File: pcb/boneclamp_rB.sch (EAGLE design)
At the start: 68 parts, among them IC1 24C, U1 ADA4841-2YRZ, U2 LT1964ES5-5TRMPBF, U3 ADA4841-2YRZ, U4 TLV70245DBVT, U5 ADA4841-2YRZ, U6 ADA4841-2YRZ, U7 AD7682BCPZ, U8 TPS63700DRCT, U9 ADA4841-2YRZ

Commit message: Finished basic ADC module
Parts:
- removed C1, C2, C3, C4: 1 uF, rcl:C-EUC0402
- removed JP2: (no value), jumper:JP2E
- removed JP3, JP4: (no value), jumper:JP1E
- removed U3, U5, U6: ADA4841-2YRZ, analog-devices-01:ADA4841-2YRZ
- added C10, C11: 10uF, rcl:C-EUC0805
- added C12, C13, C14: 0.1uF, rcl:C-EUC0805
- added R14: 1k, resistor:R-US_R0805
- added SJ6: (no value), jumper:SJ
- U1: value ADA4841-2YRZ -> AD8031ARTZ-R2; device analog-devices-01:ADA4841-2YRZ -> analog-devices-01:AD8031ARTZ-R2
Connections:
- net SDIN_BB renamed DAC_SDI
- net SDIN_DC renamed DAC_SDID
- net SDO_DC renamed DAC_SDO
- removed net N$1: U3.+VS, U5.+VS
- removed net N$13: C4.1
- removed net N$15: U3.OUT1, U5.OUT1
- removed net N$2: U3.+IN1, U5.+IN1
- removed net N$20: JP3.1
- removed net N$24: JP4.1, U$42.VREF
- removed net N$26: U3.OUT2, U5.OUT2
- removed net N$3: U3.-IN1, U5.-IN1
- removed net N$4: U3.+IN2, U5.+IN2
- removed net N$5: U3.-IN2, U5.-IN2
- removed net N$6: U3.-VS, U5.-VS
- removed net VREF_2.5V: JP3.2, JP4.2
- new net ADC_SDO: SJ6.2
- new net N$28: C11.1, R14.2, U7.REF
- new net N$29: C10.1, R14.1, U1.+IN
- new net N$34: C14.1, U7.REFIN
- new net VCOM: U7.COM
- new net VREF: U1.-IN, U1.VOUT
- new net _ADC_A: U7.IN0
- new net _ADC_B: U7.IN1
- new net _ADC_C: U7.IN2
- new net _ADC_D: U7.IN3
- net AGND: now also C10.2, C11.2, C12.2, C13.2, C14.2, U1.-VS, U7.EP, U7.GND, U7.GND_2; no longer C1.2, C2.2, C3.2, C4.2
- net DGND: no longer JP2.3
- net N$10: now also U7.SCK; no longer C2.1
- net N$11: now also U7.DIN; no longer C1.1
- net N$12: now also U7.CNV; no longer JP2.2
- net N$9: now also SJ6.1; no longer C3.1
- net VDD: now also C13.1, U1.+VS, U7.VDD, U7.VDD_2
- net VDRIVE: now also C12.1, U7.VIO; no longer JP2.1
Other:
- moved on the sheet: U7, U9

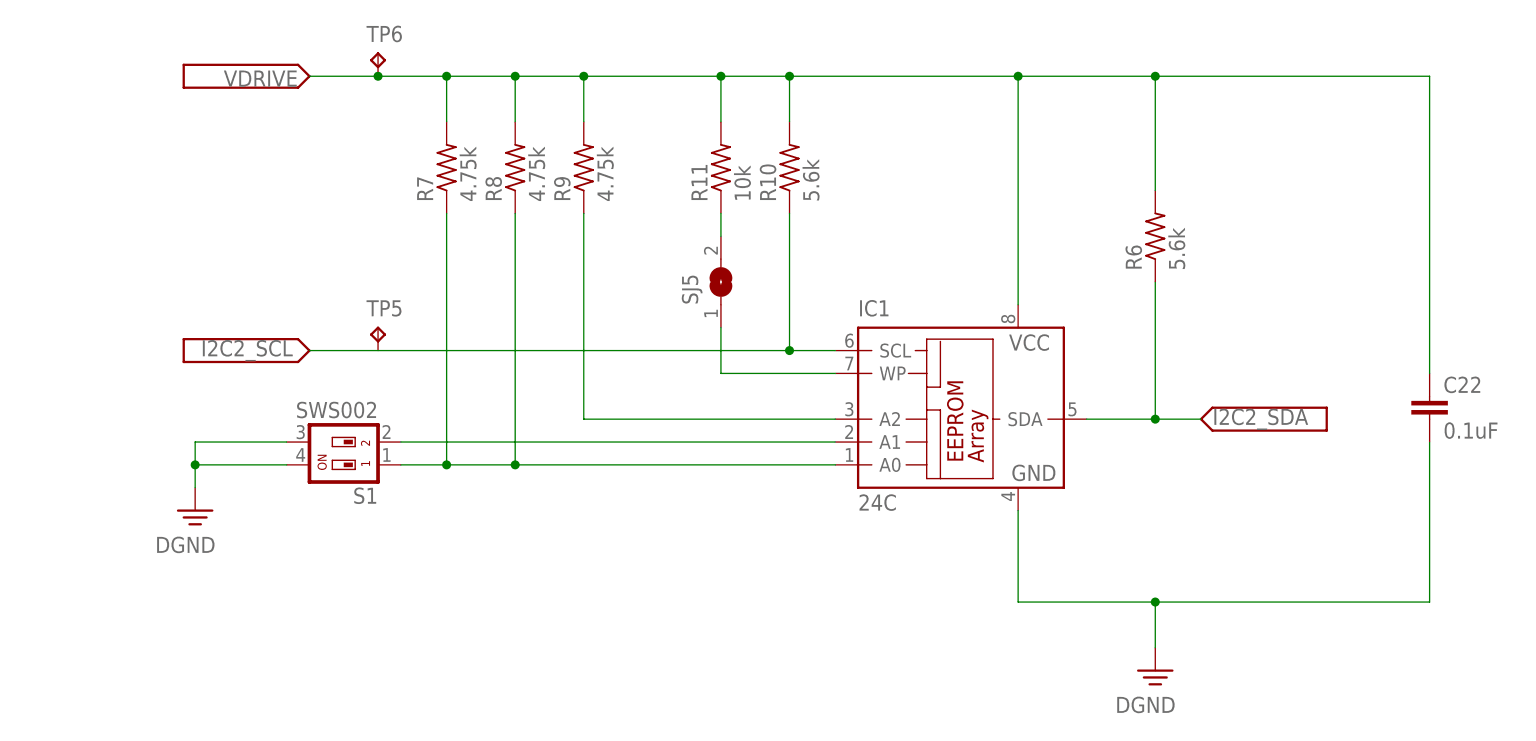
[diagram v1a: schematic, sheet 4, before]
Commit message: Added buffered VREF divider, which feeds back into ADC to get bipolar input swing.
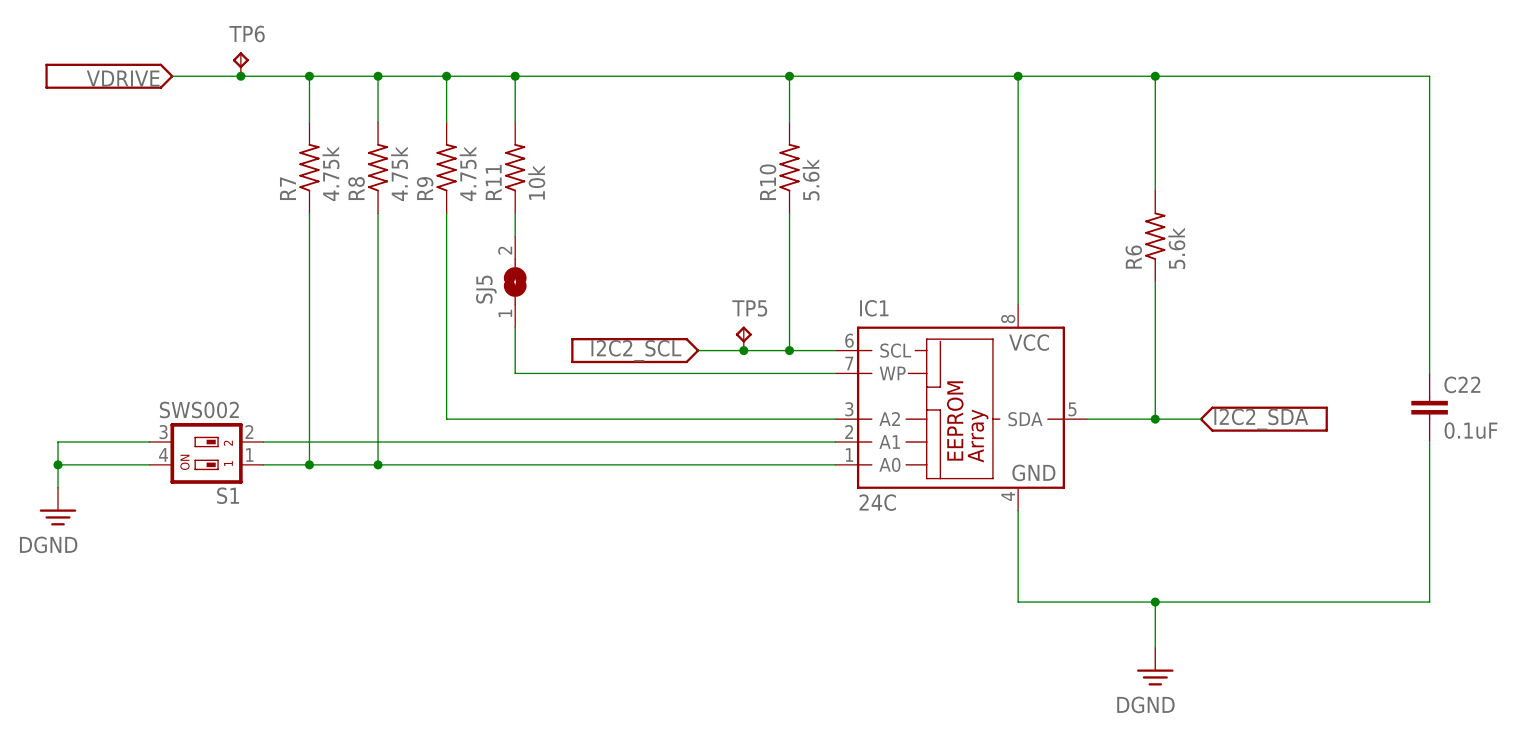
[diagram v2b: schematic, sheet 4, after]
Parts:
- added C1: 10uF, rcl:C-EUC0805
- added R15, R16: 10k,1%, resistor:R-US_R0805
- U1: value AD8031ARTZ-R2 -> AD8032ARZ-REEL7; device analog-devices-01:AD8031ARTZ-R2 -> analog-devices-02:AD8032ARZ-REEL7
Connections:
- new net N$4: C1.1, R15.2, R16.1, U1.+IN2
- net AGND: now also C1.2, R16.2
- net I2C2_SCL: now also TP5.TP
- net N$29: now also U1.+IN1; no longer U1.+IN
- net VCOM: now also U1.-IN2, U1.OUT2
- net VREF: now also R15.1, U1.-IN1, U1.OUT1; no longer U1.-IN, U1.VOUT
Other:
- moved on the sheet: C10, C11, C14, R11, R7, R8, R9, S1, SJ5, TP5, TP6

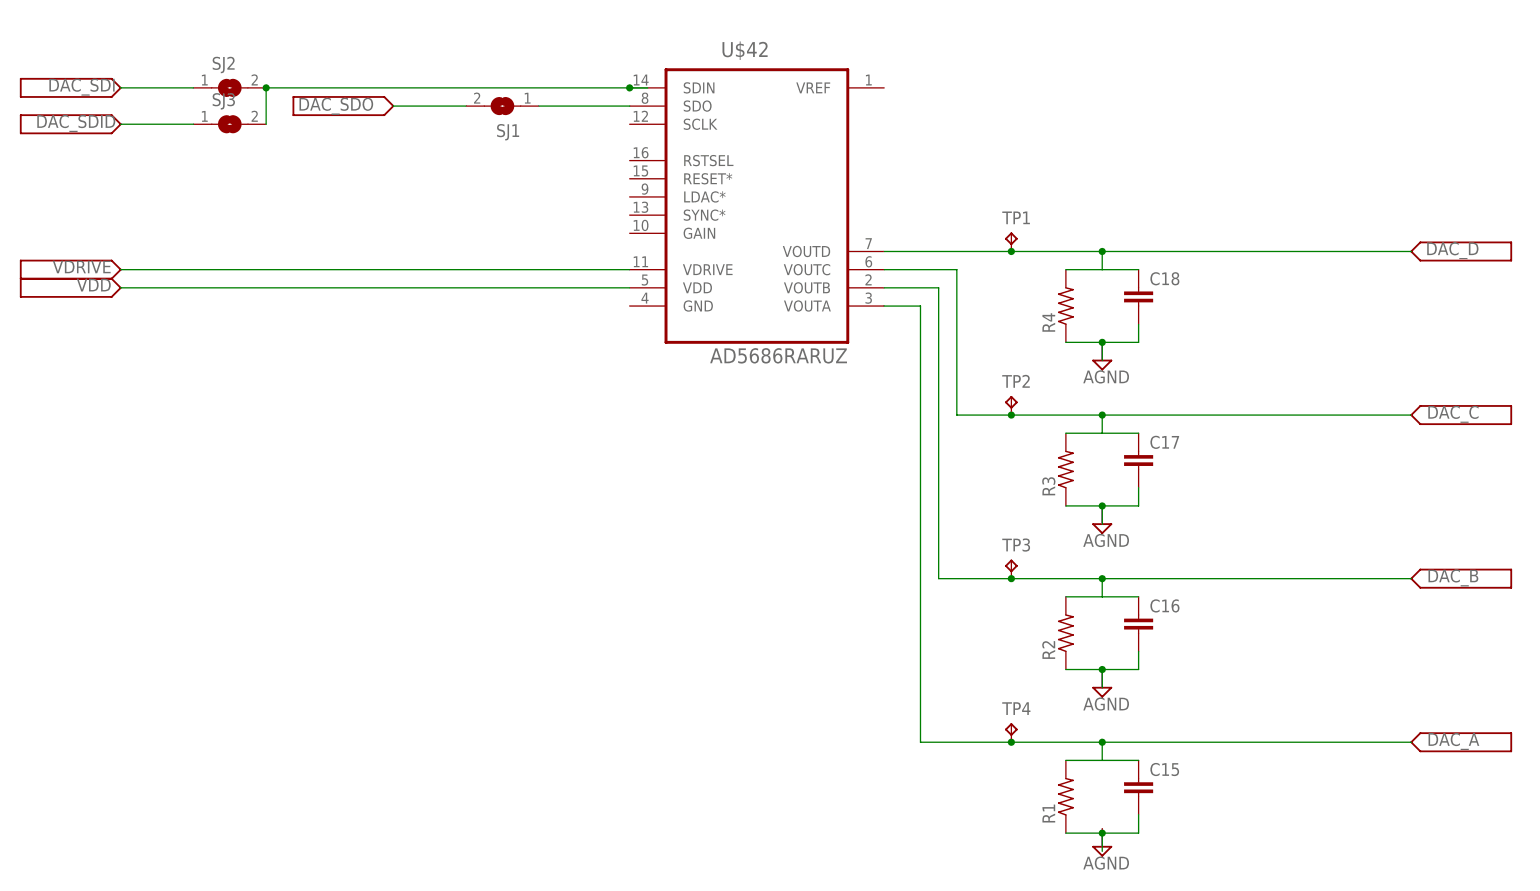
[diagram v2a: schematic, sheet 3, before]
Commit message: Finished digital input to DAC
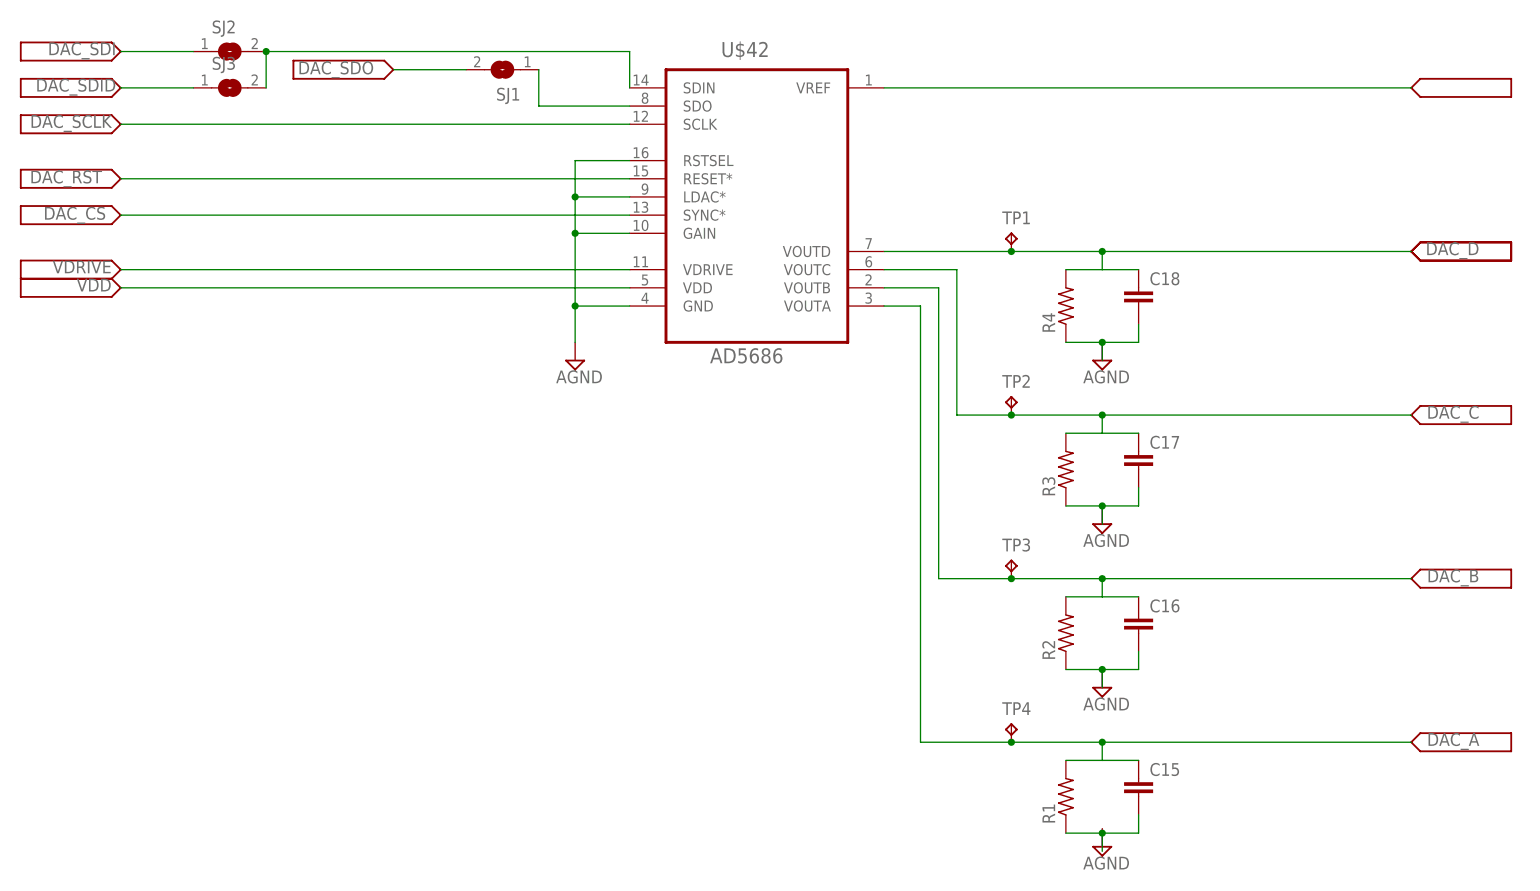
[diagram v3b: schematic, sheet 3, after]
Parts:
- added SJ7, SJ8: (no value), jumper:SJ
- U$42: value AD5686RARUZ -> AD5686
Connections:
- net N$10 renamed ADC_SCLK
- new net ADC_SDI: SJ7.1
- new net ADC_SDID: SJ8.1
- new net DAC_CS: U$42.SYNC*
- new net DAC_RST: U$42.RESET*
- new net DAC_SCLK: U$42.SCLK
- net AGND: now also U$42.GAIN, U$42.GND, U$42.LDAC*, U$42.RSTSEL
- net N$11: now also SJ7.2, SJ8.2
- net VREF: now also U$42.VREF
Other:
- moved on the sheet: C14, SJ1, SJ2, SJ3, U9

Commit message: Minor schematic edit
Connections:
- new net _DAC_A: C15.1, R1.2, TP4.TP, U$42.VOUTA
- new net _DAC_B: C16.1, R2.2, TP3.TP, U$42.VOUTB
- new net _DAC_C: C17.1, R3.2, TP2.TP, U$42.VOUTC
- new net _DAC_D: C18.1, R4.2, TP1.TP, U$42.VOUTD
- net DAC_A: no longer C15.1, R1.2, TP4.TP, U$42.VOUTA
- net DAC_B: no longer C16.1, R2.2, TP3.TP, U$42.VOUTB
- net DAC_C: no longer C17.1, R3.2, TP2.TP, U$42.VOUTC
- net DAC_D: no longer C18.1, R4.2, TP1.TP, U$42.VOUTD
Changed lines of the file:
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@@
 </busses>
 <nets>
-<net name="DAC_A" class="0">
-<segment>
-<wire x1="17.78" y1="-15.24" x2="22.86" y2="-15.24" width="0.1524" layer="91"/>
-<label x="100.965" y="-74.93" size="1.778" layer="95" rot="R180"/>
-<wire x1="22.86" y1="-15.24" x2="22.86" y2="-76.2" width="0.1524" layer="91"/>
-<wire x1="22.86" y1="-76.2" x2="35.56" y2="-76.2" width="0.1524" layer="91"/>
-<pinref part="R1" gate="G$1" pin="2"/>
-<pinref part="C15" gate="G$1" pin="1"/>
-<wire x1="35.56" y1="-76.2" x2="48.26" y2="-76.2" width="0.1524" layer="91"/>
-<wire x1="48.26" y1="-76.2" x2="91.44" y2="-76.2" width="0.1524" layer="91"/>
-<wire x1="48.26" y1="-78.74" x2="53.34" y2="-78.74" width="0.1524" layer="91"/>
-<wire x1="43.18" y1="-78.74" x2="48.26" y2="-78.74" width="0.1524" layer="91"/>
-<wire x1="48.26" y1="-78.74" x2="48.26" y2="-76.2" width="0.1524" layer="91"/>
-<junction x="48.26" y="-76.2"/>
-<pinref part="TP4" gate="G$1" pin="TP"/>
-<junction x="35.56" y="-76.2"/>
-<pinref part="U$42" gate="G$1" pin="VOUTA"/>
-</segment>
-</net>
-<net name="DAC_B" class="0">
-<segment>
-<pinref part="R2" gate="G$1" pin="2"/>
-<pinref part="C16" gate="G$1" pin="1"/>
-<wire x1="48.26" y1="-55.88" x2="53.34" y2="-55.88" width="0.1524" layer="91"/>
-<wire x1="43.18" y1="-55.88" x2="48.26" y2="-55.88" width="0.1524" layer="91"/>
-<wire x1="48.26" y1="-55.88" x2="48.26" y2="-53.34" width="0.1524" layer="91"/>
-<wire x1="17.78" y1="-12.7" x2="25.4" y2="-12.7" width="0.1524" layer="91"/>
-<wire x1="25.4" y1="-12.7" x2="25.4" y2="-53.34" width="0.1524" layer="91"/>
-<wire x1="25.4" y1="-53.34" x2="35.56" y2="-53.34" width="0.1524" layer="91"/>
-<wire x1="35.56" y1="-53.34" x2="48.26" y2="-53.34" width="0.1524" layer="91"/>
-<wire x1="48.26" y1="-53.34" x2="91.44" y2="-53.34" width="0.1524" layer="91"/>
-<junction x="48.26" y="-53.34"/>
-<label x="100.965" y="-52.07" size="1.778" layer="95" rot="R180"/>
-<pinref part="TP3" gate="G$1" pin="TP"/>
-<junction x="35.56" y="-53.34"/>
-<pinref part="U$42" gate="G$1" pin="VOUTB"/>
-</segment>
-</net>
 <net name="N$7" class="0">
 <segment>
@@
 </segment>
 </net>
-<net name="DAC_C" class="0">
+<net name="VREF" class="0">
+<segment>
+<pinref part="U$42" gate="G$1" pin="VREF"/>
+<wire x1="17.78" y1="15.24" x2="91.44" y2="15.24" width="0.1524" layer="91"/>
+<label x="92.71" y="14.605" size="1.778" layer="95"/>
+</segment>
+</net>
+<net name="DAC_SCLK" class="0">
+<segment>
+<pinref part="U$42" gate="G$1" pin="SCLK"/>
+<wire x1="-17.78" y1="10.16" x2="-88.9" y2="10.16" width="0.1524" layer="91"/>
+<label x="-90.17" y="11.43" size="1.778" layer="95" rot="R180"/>
+</segment>
+</net>
+<net name="DAC_RST" class="0">
+<segment>
+<pinref part="U$42" gate="G$1" pin="RESET*"/>
+<wire x1="-17.78" y1="2.54" x2="-88.9" y2="2.54" width="0.1524" layer="91"/>
+<label x="-101.6" y="1.905" size="1.778" layer="95"/>
+</segment>
+</net>
+<net name="DAC_CS" class="0">
+<segment>
+<pinref part="U$42" gate="G$1" pin="SYNC*"/>
+<wire x1="-88.9" y1="-2.54" x2="-17.78" y2="-2.54" width="0.1524" layer="91"/>
+<label x="-99.695" y="-3.175" size="1.778" layer="95"/>
+</segment>
+</net>
+<net name="_DAC_D" class="0">
+<segment>
+<wire x1="17.78" y1="-7.62" x2="35.56" y2="-7.62" width="0.1524" layer="91"/>
+<label x="102.87" y="-6.35" size="1.778" layer="95" rot="R180"/>
+<pinref part="R4" gate="G$1" pin="2"/>
+<pinref part="C18" gate="G$1" pin="1"/>
+<wire x1="48.26" y1="-10.16" x2="53.34" y2="-10.16" width="0.1524" layer="91"/>
+<wire x1="43.18" y1="-10.16" x2="48.26" y2="-10.16" width="0.1524" layer="91"/>
+<wire x1="48.26" y1="-10.16" x2="48.26" y2="-7.62" width="0.1524" layer="91"/>
+<wire x1="35.56" y1="-7.62" x2="48.26" y2="-7.62" width="0.1524" layer="91"/>
+<wire x1="48.26" y1="-7.62" x2="91.44" y2="-7.62" width="0.1524" layer="91"/>
+<junction x="48.26" y="-7.62"/>
+<pinref part="TP1" gate="G$1" pin="TP"/>
+<junction x="35.56" y="-7.62"/>
+<pinref part="U$42" gate="G$1" pin="VOUTD"/>
+</segment>
+</net>
+<net name="_DAC_C" class="0">
 <segment>
 <wire x1="27.94" y1="-10.16" x2="17.78" y2="-10.16" width="0.1524" layer="91"/>
-<label x="100.965" y="-29.21" size="1.778" layer="95" rot="R180"/>
+<label x="102.87" y="-29.21" size="1.778" layer="95" rot="R180"/>
 <wire x1="27.94" y1="-10.16" x2="27.94" y2="-30.48" width="0.1524" layer="91"/>
 <wire x1="27.94" y1="-30.48" x2="35.56" y2="-30.48" width="0.1524" layer="91"/>
@@
 </segment>
 </net>
-<net name="DAC_D" class="0">
-<segment>
-<wire x1="17.78" y1="-7.62" x2="35.56" y2="-7.62" width="0.1524" layer="91"/>
-<label x="100.965" y="-6.35" size="1.778" layer="95" rot="R180"/>
-<pinref part="R4" gate="G$1" pin="2"/>
-<pinref part="C18" gate="G$1" pin="1"/>
-<wire x1="48.26" y1="-10.16" x2="53.34" y2="-10.16" width="0.1524" layer="91"/>
-<wire x1="43.18" y1="-10.16" x2="48.26" y2="-10.16" width="0.1524" layer="91"/>
-<wire x1="48.26" y1="-10.16" x2="48.26" y2="-7.62" width="0.1524" layer="91"/>
-<wire x1="35.56" y1="-7.62" x2="48.26" y2="-7.62" width="0.1524" layer="91"/>
-<wire x1="48.26" y1="-7.62" x2="91.44" y2="-7.62" width="0.1524" layer="91"/>
-<junction x="48.26" y="-7.62"/>
-<pinref part="TP1" gate="G$1" pin="TP"/>
-<junction x="35.56" y="-7.62"/>
-<pinref part="U$42" gate="G$1" pin="VOUTD"/>
-</segment>
-</net>
-<net name="VREF" class="0">
-<segment>
-<pinref part="U$42" gate="G$1" pin="VREF"/>
-<wire x1="17.78" y1="15.24" x2="91.44" y2="15.24" width="0.1524" layer="91"/>
-</segment>
-</net>
-<net name="DAC_SCLK" class="0">
-<segment>
-<pinref part="U$42" gate="G$1" pin="SCLK"/>
-<wire x1="-17.78" y1="10.16" x2="-88.9" y2="10.16" width="0.1524" layer="91"/>
-<label x="-90.17" y="11.43" size="1.778" layer="95" rot="R180"/>
-</segment>
-</net>
-<net name="DAC_RST" class="0">
-<segment>
-<pinref part="U$42" gate="G$1" pin="RESET*"/>
-<wire x1="-17.78" y1="2.54" x2="-88.9" y2="2.54" width="0.1524" layer="91"/>
-<label x="-101.6" y="1.905" size="1.778" layer="95"/>
-</segment>
-</net>
-<net name="DAC_CS" class="0">
-<segment>
-<pinref part="U$42" gate="G$1" pin="SYNC*"/>
-<wire x1="-88.9" y1="-2.54" x2="-17.78" y2="-2.54" width="0.1524" layer="91"/>
-<label x="-99.695" y="-3.175" size="1.778" layer="95"/>
-</segment>
-</net>
+<net name="_DAC_B" class="0">
+<segment>
+<pinref part="R2" gate="G$1" pin="2"/>
+<pinref part="C16" gate="G$1" pin="1"/>
+<wire x1="48.26" y1="-55.88" x2="53.34" y2="-55.88" width="0.1524" layer="91"/>
+<wire x1="43.18" y1="-55.88" x2="48.26" y2="-55.88" width="0.1524" layer="91"/>
+<wire x1="48.26" y1="-55.88" x2="48.26" y2="-53.34" width="0.1524" layer="91"/>
+<wire x1="17.78" y1="-12.7" x2="25.4" y2="-12.7" width="0.1524" layer="91"/>
+<wire x1="25.4" y1="-12.7" x2="25.4" y2="-53.34" width="0.1524" layer="91"/>
+<wire x1="25.4" y1="-53.34" x2="35.56" y2="-53.34" width="0.1524" layer="91"/>
+<wire x1="35.56" y1="-53.34" x2="48.26" y2="-53.34" width="0.1524" layer="91"/>
+<wire x1="48.26" y1="-53.34" x2="91.44" y2="-53.34" width="0.1524" layer="91"/>
+<junction x="48.26" y="-53.34"/>
+<label x="102.87" y="-52.07" size="1.778" layer="95" rot="R180"/>
+<pinref part="TP3" gate="G$1" pin="TP"/>
+<junction x="35.56" y="-53.34"/>
+<pinref part="U$42" gate="G$1" pin="VOUTB"/>
+</segment>
+</net>
+<net name="_DAC_A" class="0">
+<segment>
+<wire x1="17.78" y1="-15.24" x2="22.86" y2="-15.24" width="0.1524" layer="91"/>
+<label x="102.87" y="-74.93" size="1.778" layer="95" rot="R180"/>
+<wire x1="22.86" y1="-15.24" x2="22.86" y2="-76.2" width="0.1524" layer="91"/>
+<wire x1="22.86" y1="-76.2" x2="35.56" y2="-76.2" width="0.1524" layer="91"/>
+<pinref part="R1" gate="G$1" pin="2"/>
+<pinref part="C15" gate="G$1" pin="1"/>
+<wire x1="35.56" y1="-76.2" x2="48.26" y2="-76.2" width="0.1524" layer="91"/>
+<wire x1="48.26" y1="-76.2" x2="91.44" y2="-76.2" width="0.1524" layer="91"/>
+<wire x1="48.26" y1="-78.74" x2="53.34" y2="-78.74" width="0.1524" layer="91"/>
+<wire x1="43.18" y1="-78.74" x2="48.26" y2="-78.74" width="0.1524" layer="91"/>
+<wire x1="48.26" y1="-78.74" x2="48.26" y2="-76.2" width="0.1524" layer="91"/>
+<junction x="48.26" y="-76.2"/>
+<pinref part="TP4" gate="G$1" pin="TP"/>
+<junction x="35.56" y="-76.2"/>
+<pinref part="U$42" gate="G$1" pin="VOUTA"/>
+</segment>
+</net>
